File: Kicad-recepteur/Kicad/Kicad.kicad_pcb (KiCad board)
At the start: 4 copper layers, 32.1 x 30 mm, 27 parts, among them J1 Conn_02x07_Odd_Even, J3 Conn_01x04, J4 Conn_01x02, J42 Conn_01x04, J5 USB_C_Receptacle_PowerOnly_6P, U1 STM32L021K4Tx, U2 BU33SD5WG-TR

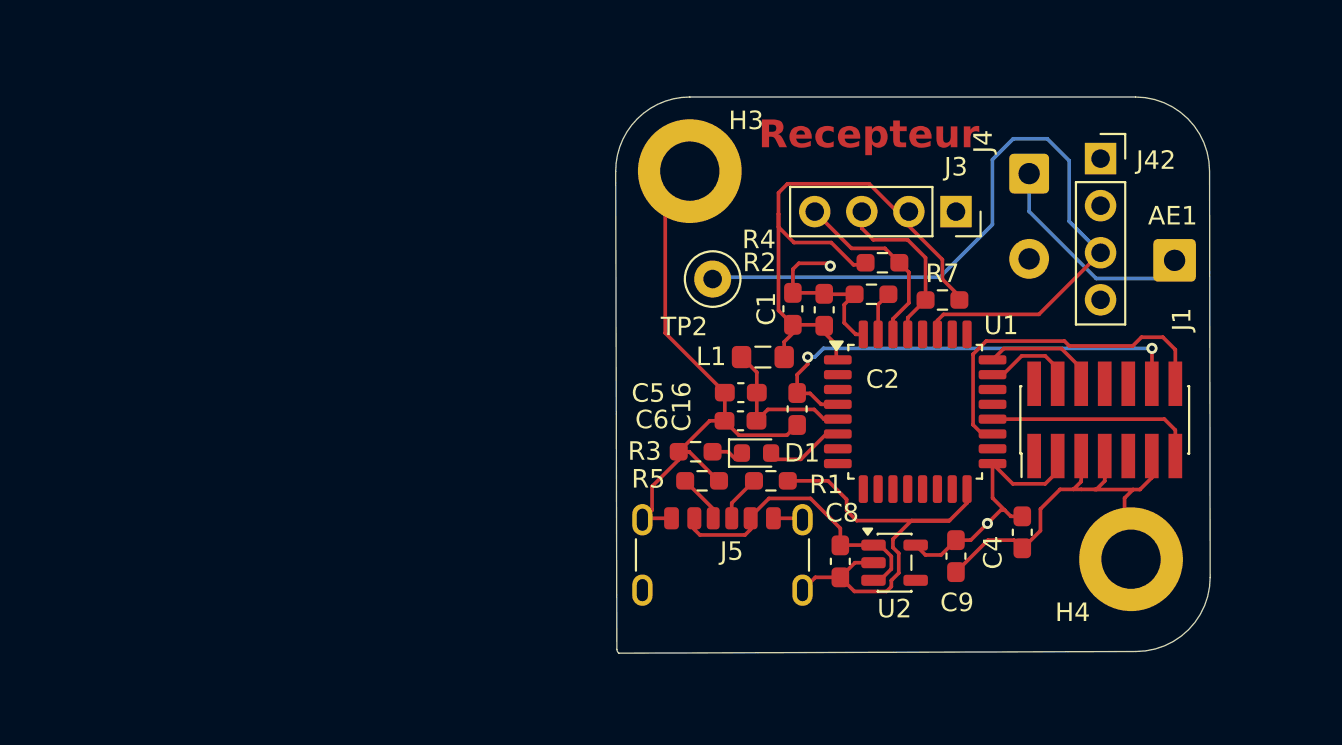
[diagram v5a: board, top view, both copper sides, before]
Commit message: feat: Add initial KiCad project preference file for the emitter and PCB layout for the receiver.
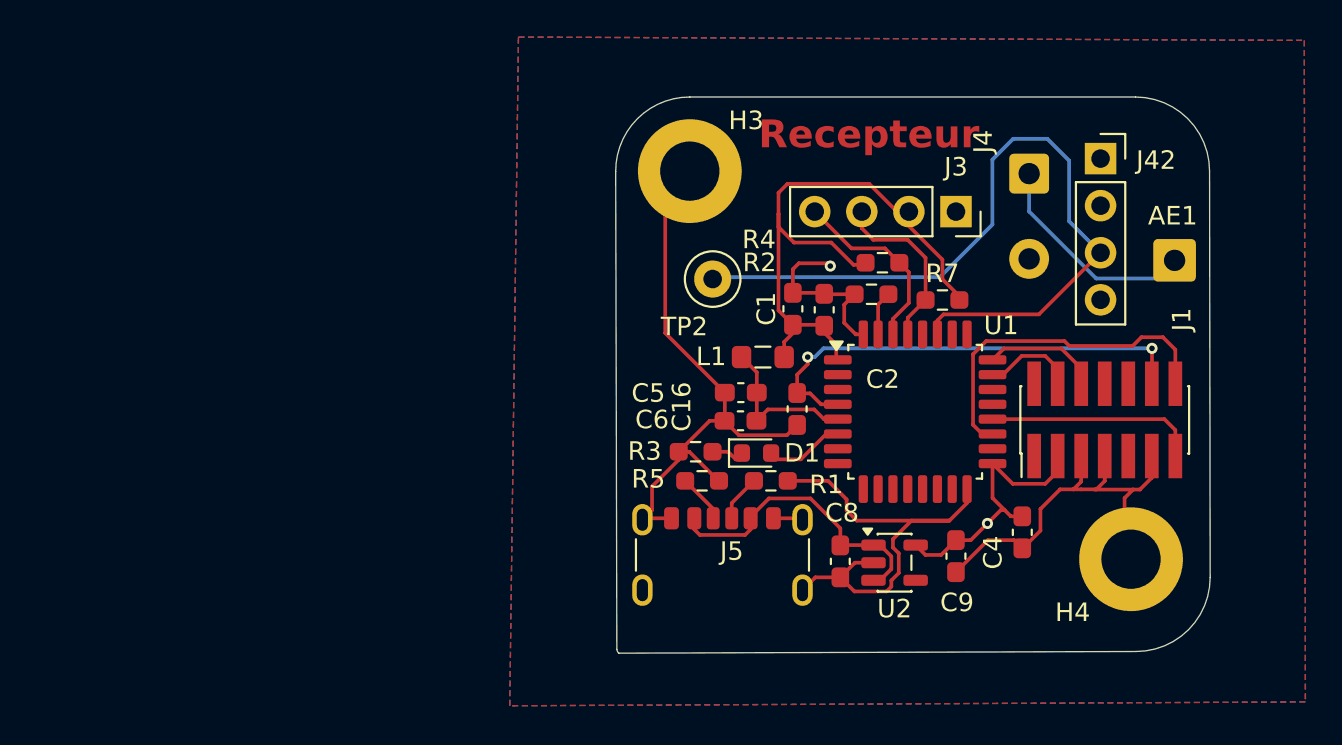
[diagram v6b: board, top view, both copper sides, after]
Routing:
- added copper zone on B.Cu, net (none)
- added copper zone on F.Cu, net (none)
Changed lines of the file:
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@@
+	)
+	(zone
+		(net 0)
+		(net_name "")
+		(layers "F.Cu" "B.Cu")
+		(hatch edge 0.5)
+		(connect_pads
+			(clearance 0.5)
+		)
+		(min_thickness 0.25)
+		(filled_areas_thickness no)
+		(fill yes
+			(thermal_gap 0.5)
+			(thermal_bridge_width 0.5)
+			(island_removal_mode 1)
+			(island_area_min 10)
+		)
+		(polygon
+			(pts
+				(xy 90.15 86.06) (xy 132.56 86.24) (xy 132.62 121.94) (xy 89.68 122.15)
+			)
+		)
 	)
 	(zone
